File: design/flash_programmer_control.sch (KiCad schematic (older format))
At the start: 16 parts, among them P301 ISP, Q301 2N3906, U301 ATMEGA328P_TQFN, U302 74HC595, U303 74HC595

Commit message: Associate footprints and correct pin orders for transistors
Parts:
- Q301: footprint (none) -> TO_SOT_Packages_SMD:SOT-23_Handsoldering
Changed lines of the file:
@@
 $EndComp
 $Comp
-L GND #PWR018
+L GND #PWR312
 U 1 1 58C24608
 P 3950 7300
-F 0 "#PWR018" H 3950 7050 50  0001 C CNN
+F 0 "#PWR312" H 3950 7050 50  0001 C CNN
 F 1 "GND" H 3950 7150 50  0000 C CNN
 F 2 "" H 3950 7300 50  0000 C CNN
@@
 $EndComp
 $Comp
-L GND #PWR019
+L GND #PWR310
 U 1 1 58C2460E
 P 3400 7300
-F 0 "#PWR019" H 3400 7050 50  0001 C CNN
+F 0 "#PWR310" H 3400 7050 50  0001 C CNN
 F 1 "GND" H 3400 7150 50  0000 C CNN
 F 2 "" H 3400 7300 50  0000 C CNN
@@
 $EndComp
 $Comp
-L VCC #PWR020
+L VCC #PWR311
 U 1 1 58C24614
 P 3950 6700
-F 0 "#PWR020" H 3950 6550 50  0001 C CNN
+F 0 "#PWR311" H 3950 6550 50  0001 C CNN
 F 1 "VCC" H 3950 6850 50  0000 C CNN
 F 2 "" H 3950 6700 50  0000 C CNN
@@
 $EndComp
 $Comp
-L VCC #PWR021
+L VCC #PWR309
 U 1 1 58C2461A
 P 3400 6700
-F 0 "#PWR021" H 3400 6550 50  0001 C CNN
+F 0 "#PWR309" H 3400 6550 50  0001 C CNN
 F 1 "VCC" H 3400 6850 50  0000 C CNN
 F 2 "" H 3400 6700 50  0000 C CNN
@@
 $EndComp
 $Comp
-L VCC #PWR022
+L VCC #PWR320
 U 1 1 58C2462B
 P 6450 2000
-F 0 "#PWR022" H 6450 1850 50  0001 C CNN
+F 0 "#PWR320" H 6450 1850 50  0001 C CNN
 F 1 "VCC" H 6450 2150 50  0000 C CNN
 F 2 "" H 6450 2000 50  0000 C CNN
@@
 	2400 2200 2300 2200
 $Comp
-L VCC #PWR023
+L VCC #PWR304
 U 1 1 58C24644
 P 2300 2200
-F 0 "#PWR023" H 2300 2050 50  0001 C CNN
+F 0 "#PWR304" H 2300 2050 50  0001 C CNN
 F 1 "VCC" H 2300 2350 50  0000 C CNN
 F 2 "" H 2300 2200 50  0000 C CNN
@@
 $EndComp
 $Comp
-L VCC #PWR024
+L VCC #PWR303
 U 1 1 58C2464A
 P 2300 2000
-F 0 "#PWR024" H 2300 1850 50  0001 C CNN
+F 0 "#PWR303" H 2300 1850 50  0001 C CNN
 F 1 "VCC" H 2300 2150 50  0000 C CNN
 F 2 "" H 2300 2000 50  0000 C CNN
@@
 $EndComp
 $Comp
-L GND #PWR025
+L GND #PWR302
 U 1 1 58C24650
 P 2100 2100
-F 0 "#PWR025" H 2100 1850 50  0001 C CNN
+F 0 "#PWR302" H 2100 1850 50  0001 C CNN
 F 1 "GND" H 2100 1950 50  0000 C CNN
 F 2 "" H 2100 2100 50  0000 C CNN
@@
 $EndComp
 $Comp
-L GND #PWR026
+L GND #PWR301
 U 1 1 58C24656
 P 2100 1900
-F 0 "#PWR026" H 2100 1650 50  0001 C CNN
+F 0 "#PWR301" H 2100 1650 50  0001 C CNN
 F 1 "GND" H 2100 1750 50  0000 C CNN
 F 2 "" H 2100 1900 50  0000 C CNN
@@
 $EndComp
 $Comp
-L GND #PWR027
+L GND #PWR314
 U 1 1 58C2465C
 P 5000 2900
-F 0 "#PWR027" H 5000 2650 50  0001 C CNN
+F 0 "#PWR314" H 5000 2650 50  0001 C CNN
 F 1 "GND" H 5000 2750 50  0000 C CNN
 F 2 "" H 5000 2900 50  0000 C CNN
@@
 $EndComp
 $Comp
-L VCC #PWR028
+L VCC #PWR315
 U 1 1 58C24662
 P 5000 3200
-F 0 "#PWR028" H 5000 3050 50  0001 C CNN
+F 0 "#PWR315" H 5000 3050 50  0001 C CNN
 F 1 "VCC" H 5000 3350 50  0000 C CNN
 F 2 "" H 5000 3200 50  0000 C CNN
@@
 	3250 1200 3150 1200
 $Comp
-L GND #PWR029
+L GND #PWR308
 U 1 1 58C2469D
 P 3150 1200
-F 0 "#PWR029" H 3150 950 50  0001 C CNN
+F 0 "#PWR308" H 3150 950 50  0001 C CNN
 F 1 "GND" H 3150 1050 50  0000 C CNN
 F 2 "" H 3150 1200 50  0000 C CNN
@@
 $EndComp
 $Comp
-L GND #PWR030
+L GND #PWR307
 U 1 1 58C246B1
 P 2850 7300
-F 0 "#PWR030" H 2850 7050 50  0001 C CNN
+F 0 "#PWR307" H 2850 7050 50  0001 C CNN
 F 1 "GND" H 2850 7150 50  0000 C CNN
 F 2 "" H 2850 7300 50  0000 C CNN
@@
 $EndComp
 $Comp
-L VCC #PWR031
+L VCC #PWR306
 U 1 1 58C246B7
 P 2850 6700
-F 0 "#PWR031" H 2850 6550 50  0001 C CNN
+F 0 "#PWR306" H 2850 6550 50  0001 C CNN
 F 1 "VCC" H 2850 6850 50  0000 C CNN
 F 2 "" H 2850 6700 50  0000 C CNN
@@
 	9450 5350 9450 5450
 $Comp
-L VCC #PWR032
+L VCC #PWR322
 U 1 1 58C24A0F
 P 9450 5050
-F 0 "#PWR032" H 9450 4900 50  0001 C CNN
+F 0 "#PWR322" H 9450 4900 50  0001 C CNN
 F 1 "VCC" H 9450 5200 50  0000 C CNN
 F 2 "" H 9450 5050 50  0000 C CNN
@@
 $EndComp
 $Comp
-L GND #PWR033
+L GND #PWR323
 U 1 1 58C24A15
 P 9450 5450
-F 0 "#PWR033" H 9450 5200 50  0001 C CNN
+F 0 "#PWR323" H 9450 5200 50  0001 C CNN
 F 1 "GND" H 9450 5300 50  0000 C CNN
 F 2 "" H 9450 5450 50  0000 C CNN
@@
 $EndComp
 $Comp
-L VCC #PWR034
+L VCC #PWR321
 U 1 1 58C24FE2
 P 7550 2250
-F 0 "#PWR034" H 7550 2100 50  0001 C CNN
+F 0 "#PWR321" H 7550 2100 50  0001 C CNN
 F 1 "VCC" H 7550 2400 50  0000 C CNN
 F 2 "" H 7550 2250 50  0000 C CNN
@@
 $EndComp
 $Comp
-L GND #PWR035
+L GND #PWR317
 U 1 1 58C25028
 P 5500 7300
-F 0 "#PWR035" H 5500 7050 50  0001 C CNN
+F 0 "#PWR317" H 5500 7050 50  0001 C CNN
 F 1 "GND" H 5500 7150 50  0000 C CNN
 F 2 "" H 5500 7300 50  0000 C CNN
@@
 $EndComp
 $Comp
-L VCC #PWR036
+L VCC #PWR316
 U 1 1 58C2502E
 P 5500 6700
-F 0 "#PWR036" H 5500 6550 50  0001 C CNN
+F 0 "#PWR316" H 5500 6550 50  0001 C CNN
 F 1 "VCC" H 5500 6850 50  0000 C CNN
 F 2 "" H 5500 6700 50  0000 C CNN
@@
 $EndComp
 $Comp
-L GND #PWR037
+L GND #PWR319
 U 1 1 58C25042
 P 6100 7300
-F 0 "#PWR037" H 6100 7050 50  0001 C CNN
+F 0 "#PWR319" H 6100 7050 50  0001 C CNN
 F 1 "GND" H 6100 7150 50  0000 C CNN
 F 2 "" H 6100 7300 50  0000 C CNN
@@
 $EndComp
 $Comp
-L VCC #PWR038
+L VCC #PWR318
 U 1 1 58C25048
 P 6100 6700
-F 0 "#PWR038" H 6100 6550 50  0001 C CNN
+F 0 "#PWR318" H 6100 6550 50  0001 C CNN
 F 1 "VCC" H 6100 6850 50  0000 C CNN
 F 2 "" H 6100 6700 50  0000 C CNN
@@
 	3150 4950 3000 4950
 $Comp
-L GND #PWR039
+L GND #PWR313
 U 1 1 58C2D7C9
 P 4200 4950
-F 0 "#PWR039" H 4200 4700 50  0001 C CNN
+F 0 "#PWR313" H 4200 4700 50  0001 C CNN
 F 1 "GND" H 4200 4800 50  0000 C CNN
 F 2 "" H 4200 4950 50  0000 C CNN
@@
 	3450 4950 3700 4950
 $Comp
-L VCC #PWR040
+L VCC #PWR305
 U 1 1 58C2D7D9
 P 2550 4950
-F 0 "#PWR040" H 2550 4800 50  0001 C CNN
+F 0 "#PWR305" H 2550 4800 50  0001 C CNN
 F 1 "VCC" H 2550 5100 50  0000 C CNN
 F 2 "" H 2550 4950 50  0000 C CNN
@@
 F 0 "Q301" V 3850 5150 50  0000 L CNN
 F 1 "2N3906" V 4100 4900 50  0000 L CNN
-F 2 "" H 4100 5150 50  0000 C CNN
+F 2 "TO_SOT_Packages_SMD:SOT-23_Handsoldering" H 4100 5150 50  0001 C CNN
 F 3 "" H 3900 5050 50  0000 C CNN
 	1    3900 5050

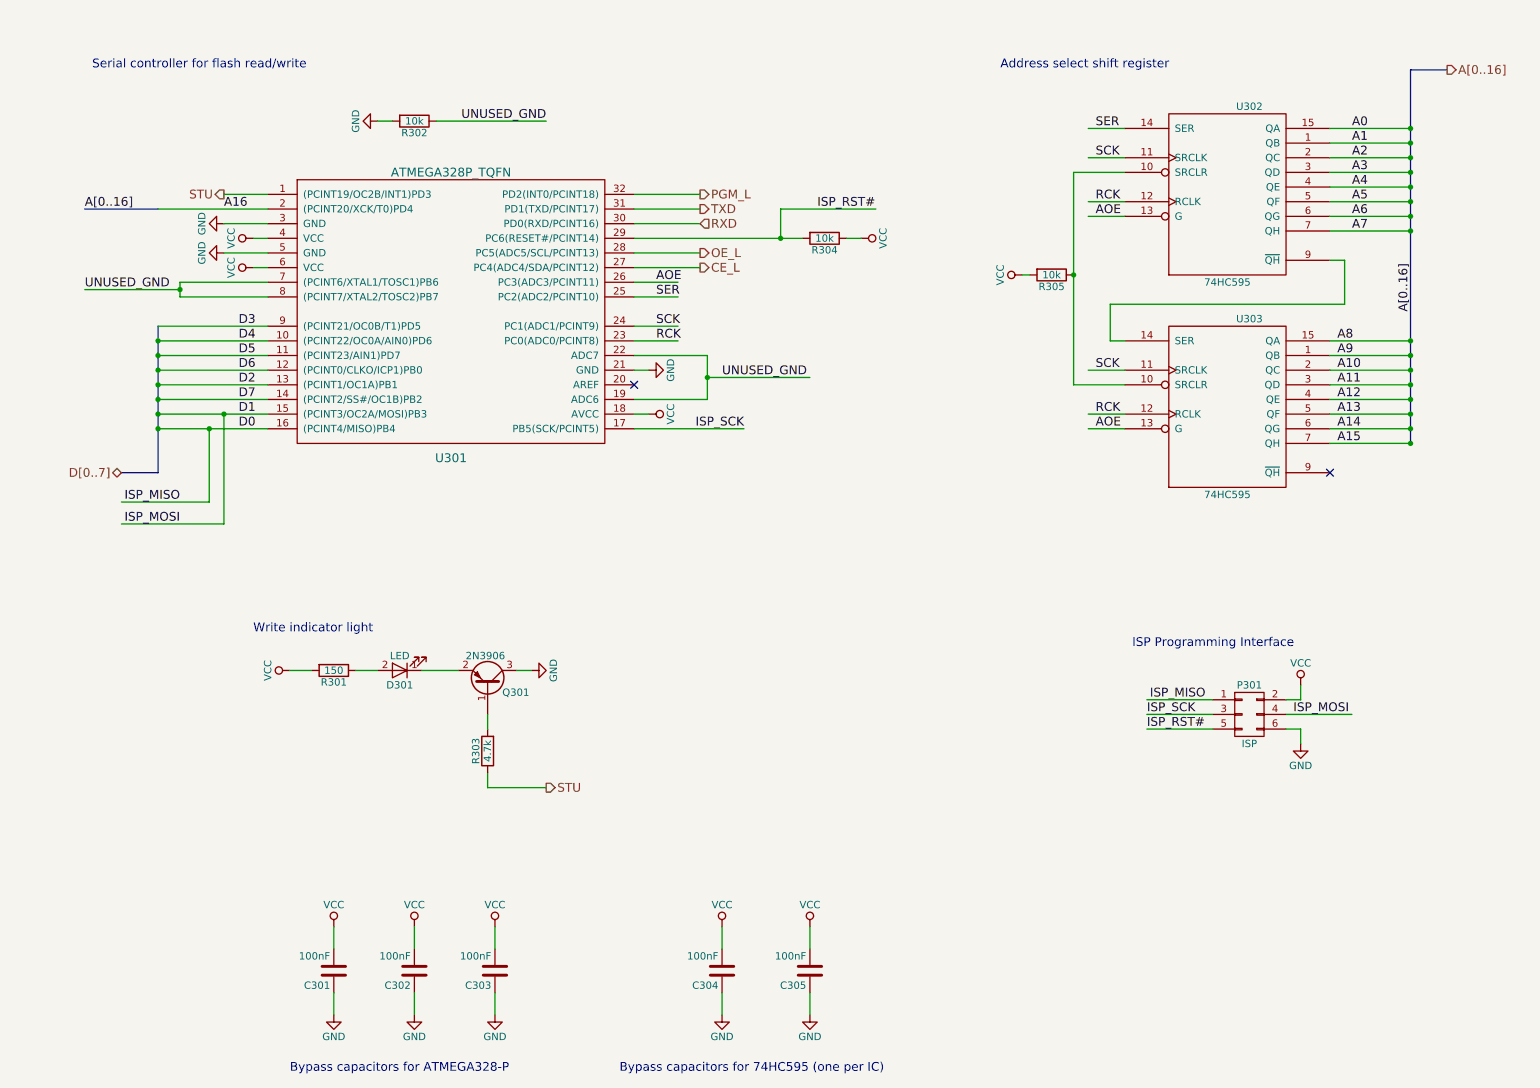
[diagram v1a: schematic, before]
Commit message: Bug fix and more schematic cleanup
The A9_VPP circuit wouldn't work in all cases, so I completely redid it and
it's simpler now.

Also started splitting up the schematic into even more sheets, and sprinkled in
some TODO comments.
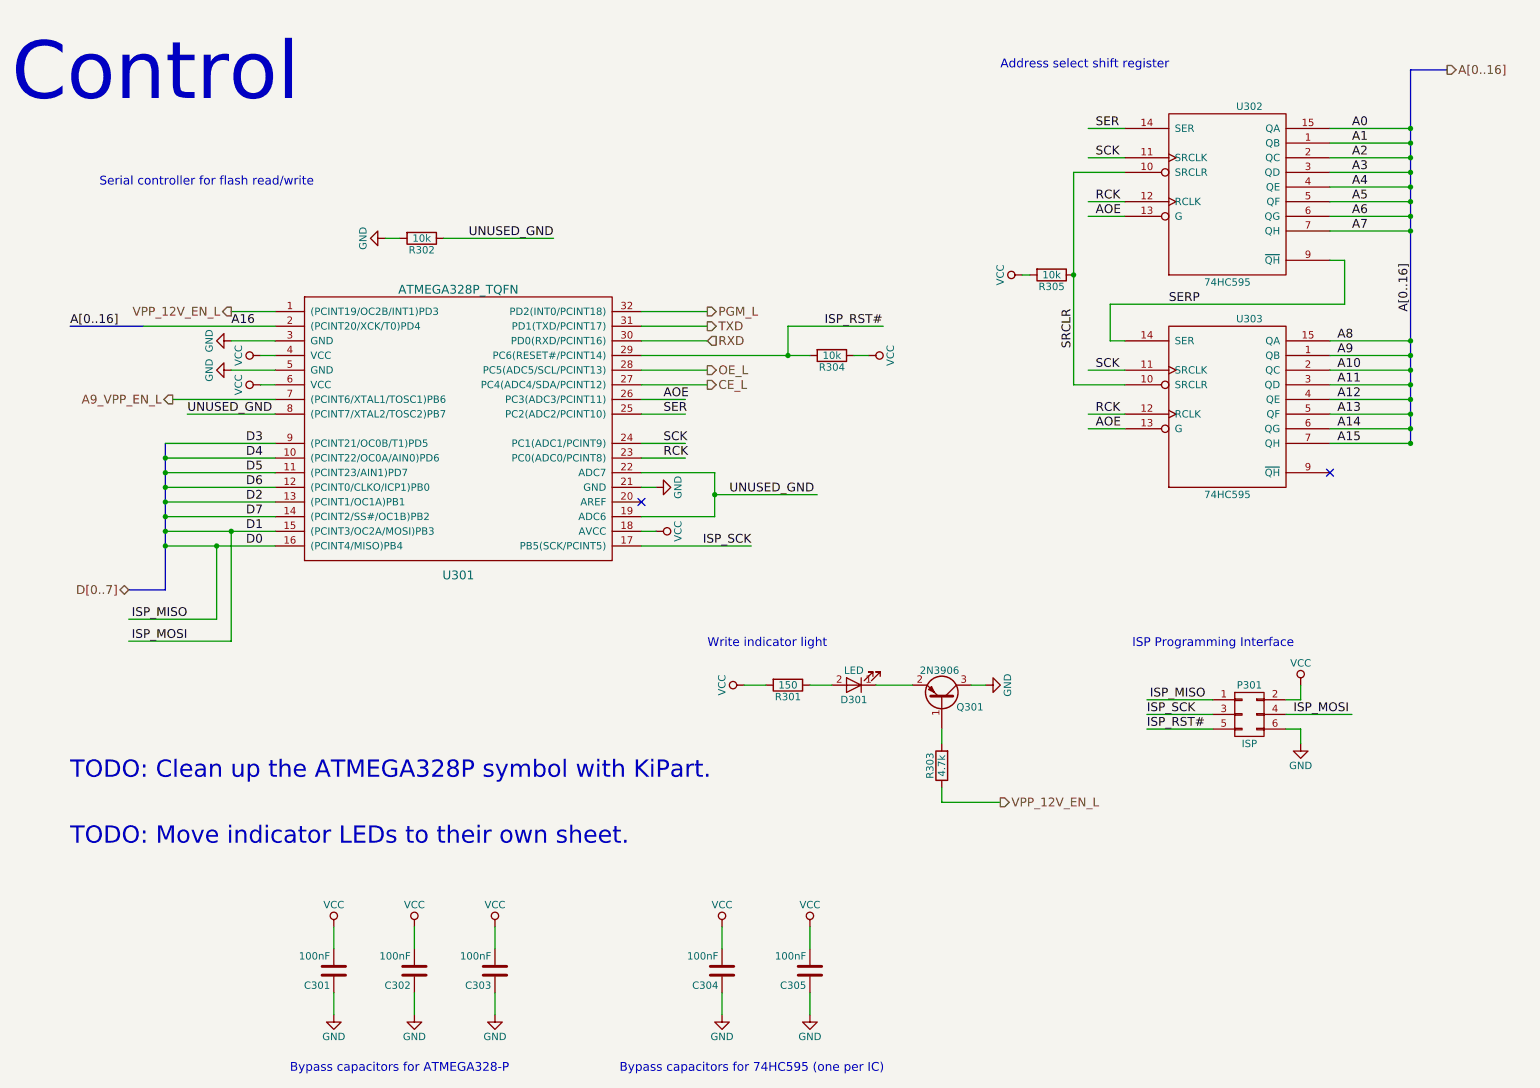
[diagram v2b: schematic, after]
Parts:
- C301, C302, C303, C304, C305: footprint Capacitors_SMD:C_0805_HandSoldering -> Resistors_SMD:R_0805_HandSoldering
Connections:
- net labels added: A9_VPP_EN_L, SERP, SRCLR, VPP_12V_EN_L
- net labels removed: STU
- wire segments 101 -> 104
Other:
- note added: "Control"
- note added: "TODO: Clean up the ATMEGA328P symbol with KiPart."
- note added: "TODO: Move indicator LEDs to their own sheet."
- moved on the sheet: D301, Q301, R301, R302, R303, R304, U301

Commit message: More schematic clean up
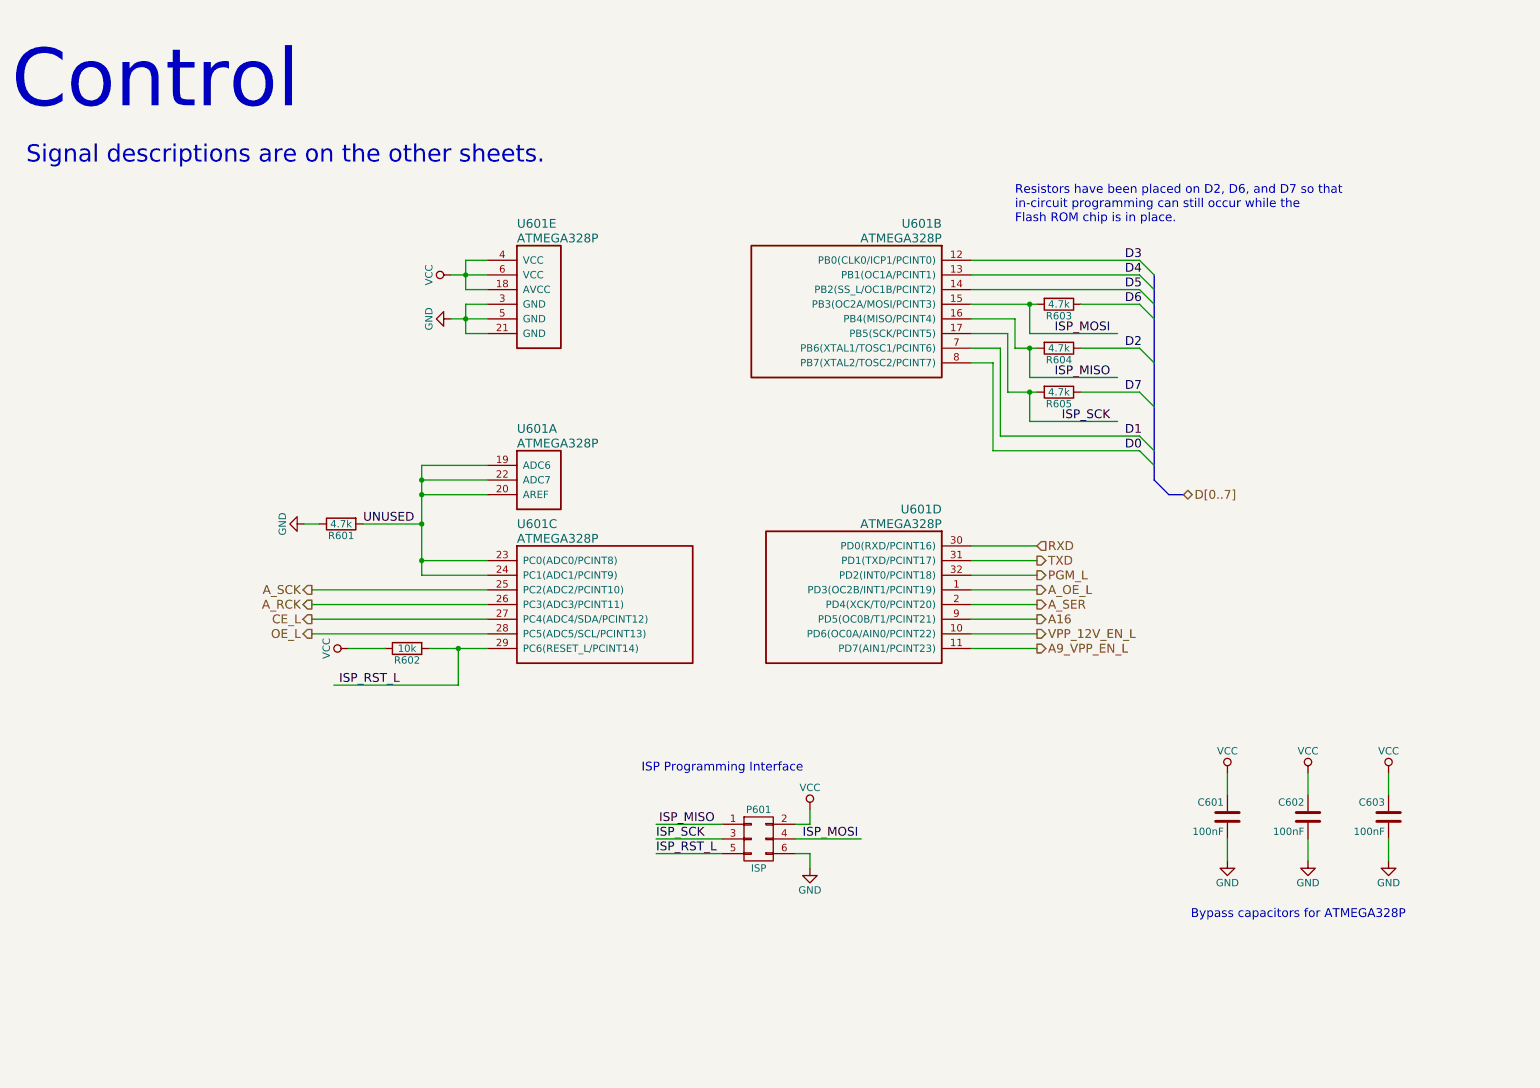
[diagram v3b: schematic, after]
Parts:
- removed C304, C305: 100nF, Resistors_SMD:R_0805_HandSoldering, symbol C
- removed D301: LED, LEDs:LED_0805, symbol LED
- removed Q301: 2N3906, TO_SOT_Packages_SMD:SOT-23_Handsoldering, symbol Q_PNP_BEC
- removed R301: 150, Resistors_SMD:R_0805_HandSoldering, symbol R
- removed R303: 4.7k, Resistors_SMD:R_0805_HandSoldering, symbol R
- removed R304, R305: 10k, Resistors_SMD:R_0805_HandSoldering, symbol R
- removed U301: ATMEGA328P_TQFN, TQFP_32_7mm_0.8mm_pitch:TQFP-32, symbol ATMEGA328P_TQFN
- removed U302, U303: 74HC595, Housings_SOIC:SOIC-16_3.9x9.9mm_Pitch1.27mm, symbol 74HC595
- added R602: 10k, Resistors_SMD:R_0603_HandSoldering, symbol R
- added R603, R604, R605: 4.7k, Resistors_SMD:R_0603_HandSoldering, symbol R
- added U601: ATMEGA328P, TQFP_32_7mm_0.8mm_pitch:TQFP-32, symbol ATMEGA328P
- C601: renamed from C301; footprint Resistors_SMD:R_0805_HandSoldering -> Resistors_SMD:R_0603_HandSoldering
- C602: renamed from C302; footprint Resistors_SMD:R_0805_HandSoldering -> Resistors_SMD:R_0603_HandSoldering
- C603: renamed from C303; footprint Resistors_SMD:R_0805_HandSoldering -> Resistors_SMD:R_0603_HandSoldering
- R601: renamed from R302; value 10k -> 4.7k; footprint Resistors_SMD:R_0805_HandSoldering -> Resistors_SMD:R_0603_HandSoldering
- renumbered P301 to P601
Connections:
- net labels added: A_OE_L, A_RCK, A_SCK, A_SER, ISP_RST_L, UNUSED
- net labels removed: A0, A1, A10, A11, A12, A13, A14, A15, A2, A3, A4, A5, A6, A7, A8, A9, AOE, A[0..16], ISP_RST#, RCK, SCK, SER, SERP, SRCLR, UNUSED_GND
- wire segments 104 -> 71
- no-connect marks 2 -> 0
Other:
- note added: "Bypass capacitors for ATMEGA328P"
- note added: "Resistors have been placed on D2, D6, and D7 so that\nin-circuit programming can still occur while the\nFlash ROM chip is in place."
- note added: "Signal descriptions are on the other sheets."
- note removed: "Address select shift register"
- note removed: "Bypass capacitors for 74HC595 (one per IC)"
- note removed: "Bypass capacitors for ATMEGA328-P"
- note removed: "Serial controller for flash read/write"
- note removed: "TODO: Clean up the ATMEGA328P symbol with KiPart."
- note removed: "TODO: Move indicator LEDs to their own sheet."
- note removed: "Write indicator light"
- moved on the sheet: C601, C602, C603, P601, R601
